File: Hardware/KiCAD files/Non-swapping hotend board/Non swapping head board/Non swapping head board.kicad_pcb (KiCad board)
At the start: 2 copper layers, 21.6 x 31.7 mm, 4 parts, among them J1 JST_06, J18 JST_1mm_3_Vertical, J20 PINHD_1x10_Female, J22 Conn_01x02

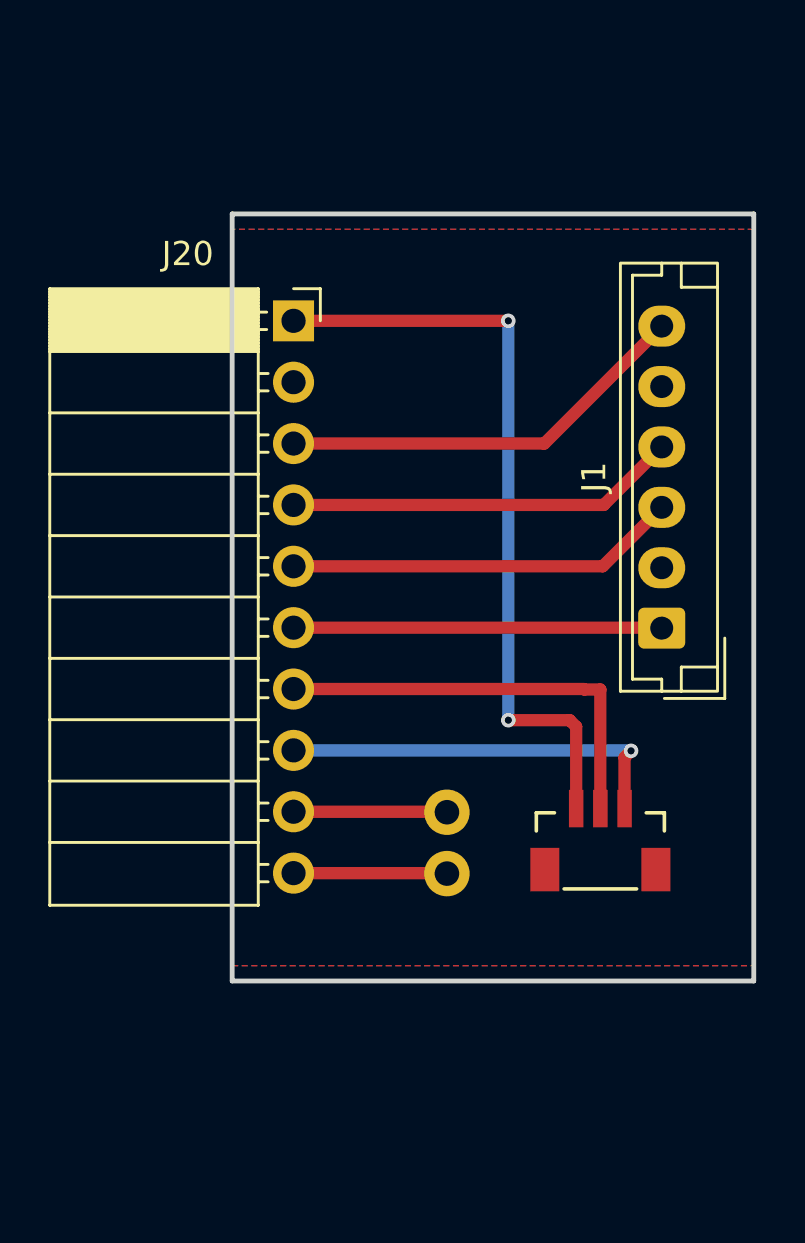
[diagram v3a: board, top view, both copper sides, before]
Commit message: Compatability mods
basic modifications to work toward compatability between boards physically on the hotend
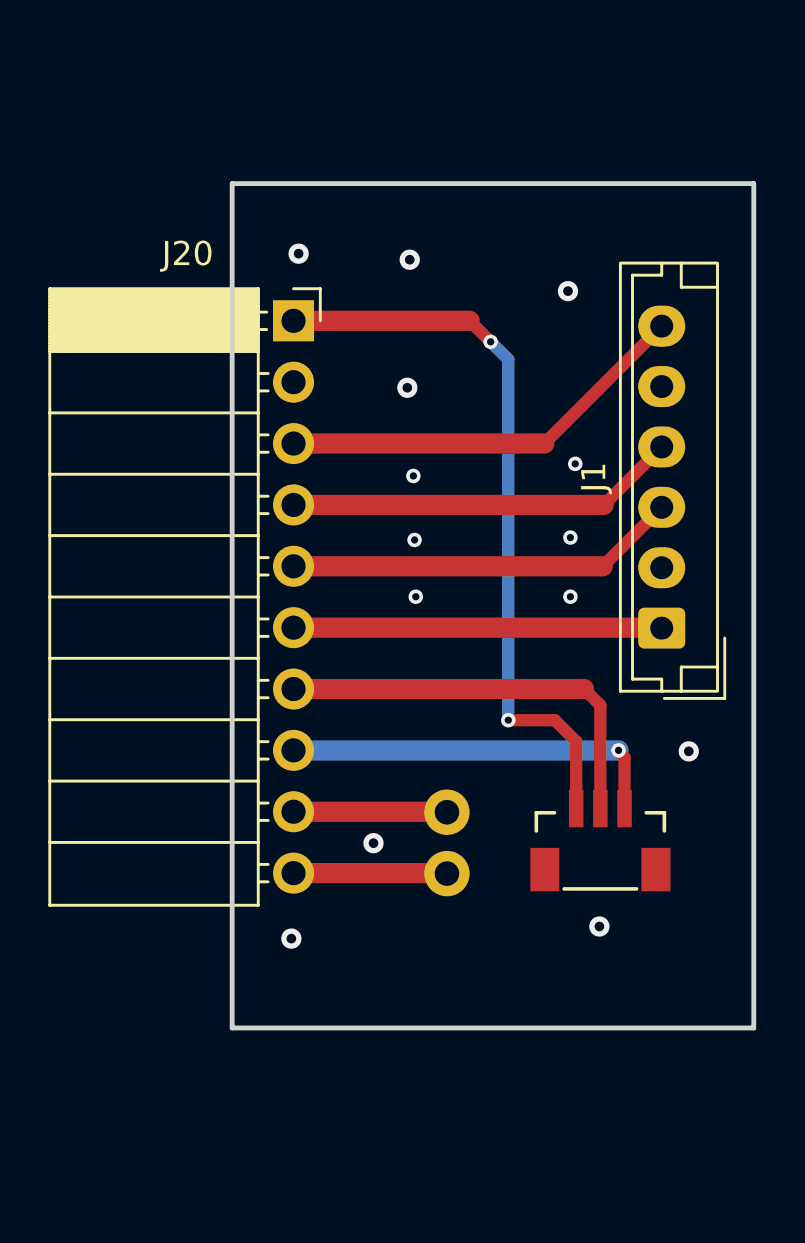
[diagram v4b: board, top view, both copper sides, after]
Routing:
- net Net-(J18-Pad3): track 31.7 -> 30.4 mm
- net Net-(J18-Pad1): track 16.5 -> 16.0 mm
- net GND: vias 0 -> 14
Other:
- board size 21.6 x 31.7 mm -> 21.6 x 35 mm
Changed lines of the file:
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@@
 	)
 	(gr_rect
-		(start 95.25 40.005)
-		(end 116.84 71.755)
+		(start 95.25 38.75)
+		(end 116.84 73.7)
 		(stroke
 			(width 0.2)
@@
 	)
 	(segment
-		(start 109.49 61.23)
-		(end 109.22 60.96)
-		(width 0.508)
-		(layer "F.Cu")
-		(net "Net-(J18-Pad3)")
-	)
-	(segment
-		(start 109.22 60.96)
+		(start 105.95 45.3)
+		(end 105.08 44.43)
+		(width 0.508)
+		(layer "F.Cu")
+		(net "Net-(J18-Pad3)")
+	)
+	(segment
+		(start 105.08 44.43)
+		(end 97.79 44.43)
+		(width 0.8382)
+		(layer "F.Cu")
+		(net "Net-(J18-Pad3)")
+	)
+	(segment
+		(start 109.49 64.6185)
+		(end 109.49 61.84)
+		(width 0.508)
+		(layer "F.Cu")
+		(net "Net-(J18-Pad3)")
+	)
+	(segment
+		(start 109.49 61.84)
+		(end 108.61 60.96)
+		(width 0.508)
+		(layer "F.Cu")
+		(net "Net-(J18-Pad3)")
+	)
+	(segment
+		(start 108.61 60.96)
 		(end 106.68 60.96)
 		(width 0.508)
@@
 		(net "Net-(J18-Pad3)")
 	)
-	(segment
-		(start 106.68 44.43)
-		(end 97.79 44.43)
-		(width 0.508)
-		(layer "F.Cu")
-		(net "Net-(J18-Pad3)")
-	)
-	(segment
-		(start 109.49 64.6185)
-		(end 109.49 61.23)
-		(width 0.508)
-		(layer "F.Cu")
-		(net "Net-(J18-Pad3)")
-	)
 	(via
 		(at 106.68 60.96)
@@
 	)
 	(via
-		(at 106.68 44.43)
-		(size 0.6)
-		(drill 0.3)
-		(layers "F.Cu" "B.Cu")
-		(net "Net-(J18-Pad3)")
-	)
-	(segment
-		(start 106.68 44.43)
+		(at 105.95 45.3)
+		(size 0.6)
+		(drill 0.3)
+		(layers "F.Cu" "B.Cu")
+		(net "Net-(J18-Pad3)")
+	)
+	(segment
+		(start 106.68 46.03)
 		(end 106.68 60.96)
 		(width 0.508)
 		(layer "B.Cu")
 		(net "Net-(J18-Pad3)")
+	)
+	(segment
+		(start 105.95 45.3)
+		(end 106.68 46.03)
+		(width 0.508)
+		(layer "B.Cu")
+		(net "Net-(J18-Pad3)")
+	)
+	(via
+		(at 110.45 69.5)
+		(size 0.8382)
+		(drill 0.4)
+		(layers "F.Cu" "B.Cu")
+		(free yes)
+		(net "GND")
+	)
+	(via
+		(at 97.7 70)
+		(size 0.8382)
+		(drill 0.4)
+		(layers "F.Cu" "B.Cu")
+		(free yes)
+		(net "GND")
+	)
+	(via
+		(at 109.25 55.85)
+		(size 0.6)
+		(drill 0.3)
+		(layers "F.Cu" "B.Cu")
+		(free yes)
+		(net "GND")
+	)
+	(via
+		(at 102.85 55.85)
+		(size 0.6)
+		(drill 0.3)
+		(layers "F.Cu" "B.Cu")
+		(free yes)
+		(net "GND")
+	)
+	(via
+		(at 102.6 41.9)
+		(size 0.8382)
+		(drill 0.4)
+		(layers "F.Cu" "B.Cu")
+		(free yes)
+		(net "GND")
+	)
+	(via
+		(at 98 41.65)
+		(size 0.8382)
+		(drill 0.4)
+		(layers "F.Cu" "B.Cu")
+		(free yes)
+		(net "GND")
+	)
+	(via
+		(at 114.15 62.25)
+		(size 0.8382)
+		(drill 0.4)
+		(layers "F.Cu" "B.Cu")
+		(free yes)
+		(net "GND")
+	)
+	(via
+		(at 102.8 53.5)
+		(size 0.6)
+		(drill 0.3)
+		(layers "F.Cu" "B.Cu")
+		(free yes)
+		(net "GND")
+	)
+	(via
+		(at 109.45 50.35)
+		(size 0.6)
+		(drill 0.3)
+		(layers "F.Cu" "B.Cu")
+		(free yes)
+		(net "GND")
+	)
+	(via
+		(at 109.25 53.4)
+		(size 0.6)
+		(drill 0.3)
+		(layers "F.Cu" "B.Cu")
+		(free yes)
+		(net "GND")
+	)
+	(via
+		(at 101.1 66.05)
+		(size 0.8382)
+		(drill 0.4)
+		(layers "F.Cu" "B.Cu")
+		(free yes)
+		(net "GND")
+	)
+	(via
+		(at 109.15 43.2)
+		(size 0.8382)
+		(drill 0.4)
+		(layers "F.Cu" "B.Cu")
+		(free yes)
+		(net "GND")
+	)
+	(via
+		(at 102.75 50.85)
+		(size 0.6)
+		(drill 0.3)
+		(layers "F.Cu" "B.Cu")
+		(free yes)
+		(net "GND")
+	)
+	(via
+		(at 102.5 47.2)
+		(size 0.8382)
+		(drill 0.4)
+		(layers "F.Cu" "B.Cu")
+		(free yes)
+		(net "GND")
 	)
 	(segment
 		(start 108.17 49.51)
 		(end 97.79 49.51)
-		(width 0.508)
+		(width 0.8382)
 		(layer "F.Cu")
 		(net "/A1")
@@
 		(start 110.63 52.05)
 		(end 97.79 52.05)
-		(width 0.508)
+		(width 0.8382)
 		(layer "F.Cu")
 		(net "/B1")
@@
 		(start 110.59 54.59)
 		(end 97.79 54.59)
-		(width 0.508)
+		(width 0.8382)
 		(layer "F.Cu")
 		(net "/A2")
@@
 		(start 113.01 57.13)
 		(end 97.79 57.13)
-		(width 0.508)
+		(width 0.8382)
 		(layer "F.Cu")
 		(net "/B2")
@@
 	)
 	(segment
-		(start 110.49 59.69)
+		(start 109.84 59.69)
 		(end 109.83 59.69)
+		(width 0.508)
+		(layer "F.Cu")
+		(net "Net-(J18-Pad2)")
+	)
+	(segment
+		(start 110.49 60.34)
+		(end 109.84 59.69)
+		(width 0.508)
+		(layer "F.Cu")
+		(net "Net-(J18-Pad2)")
+	)
+	(segment
+		(start 109.81 59.67)
+		(end 97.79 59.67)
+		(width 0.8382)
+		(layer "F.Cu")
+		(net "Net-(J18-Pad2)")
+	)
+	(segment
+		(start 110.49 64.6185)
+		(end 110.49 60.34)
 		(width 0.508)
 		(layer "F.Cu")
@@
 	)
 	(segment
-		(start 109.81 59.67)
-		(end 97.79 59.67)
-		(width 0.508)
-		(layer "F.Cu")
-		(net "Net-(J18-Pad2)")
-	)
-	(segment
-		(start 110.49 64.6185)
-		(end 110.49 59.69)
-		(width 0.508)
-		(layer "F.Cu")
-		(net "Net-(J18-Pad2)")
-	)
-	(segment
-		(start 111.49 64.6185)
+		(start 111.244 62.21)
+		(end 111.244 62.254)
+		(width 0.508)
+		(layer "F.Cu")
+		(net "Net-(J18-Pad1)")
+	)
+	(segment
+		(start 111.49 62.5)
+		(end 111.49 64.6185)
+		(width 0.508)
+		(layer "F.Cu")
+		(net "Net-(J18-Pad1)")
+	)
+	(segment
+		(start 111.244 62.254)
 		(end 111.49 62.5)
 		(width 0.508)
@@
 		(net "Net-(J18-Pad1)")
 	)
-	(segment
-		(start 111.49 62.5)
-		(end 111.76 62.23)
-		(width 0.508)
-		(layer "F.Cu")
-		(net "Net-(J18-Pad1)")
-	)
-	(via
-		(at 111.76 62.23)
-		(size 0.6)
-		(drill 0.3)
-		(layers "F.Cu" "B.Cu")
-		(net "Net-(J18-Pad1)")
-	)
-	(segment
-		(start 111.74 62.21)
+	(via
+		(at 111.244 62.21)
+		(size 0.6)
+		(drill 0.3)
+		(layers "F.Cu" "B.Cu")
+		(net "Net-(J18-Pad1)")
+	)
+	(segment
+		(start 111.244 62.21)
 		(end 97.79 62.21)
-		(width 0.508)
-		(layer "B.Cu")
-		(net "Net-(J18-Pad1)")
-	)
-	(segment
-		(start 111.76 62.23)
-		(end 111.74 62.21)
-		(width 0.508)
+		(width 0.8382)
 		(layer "B.Cu")
 		(net "Net-(J18-Pad1)")
@@
 		(start 104.12 64.75)
 		(end 97.79 64.75)
-		(width 0.508)
+		(width 0.8382)
 		(layer "F.Cu")
 		(net "Net-(J22-Pin_2)")
@@
 		(start 104.12 67.29)
 		(end 97.79 67.29)
-		(width 0.508)
+		(width 0.8382)
 		(layer "F.Cu")
 		(net "Net-(J22-Pin_1)")
@@
 		(polygon
 			(pts
-				(xy 116.84 40.64) (xy 95.25 40.64) (xy 95.25 71.12) (xy 116.84 71.12)
+				(xy 116.84 38.75) (xy 95.25 38.75) (xy 95.25 73.7) (xy 116.84 73.7)
 			)
 		)

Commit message: V1 boards after final board invoice
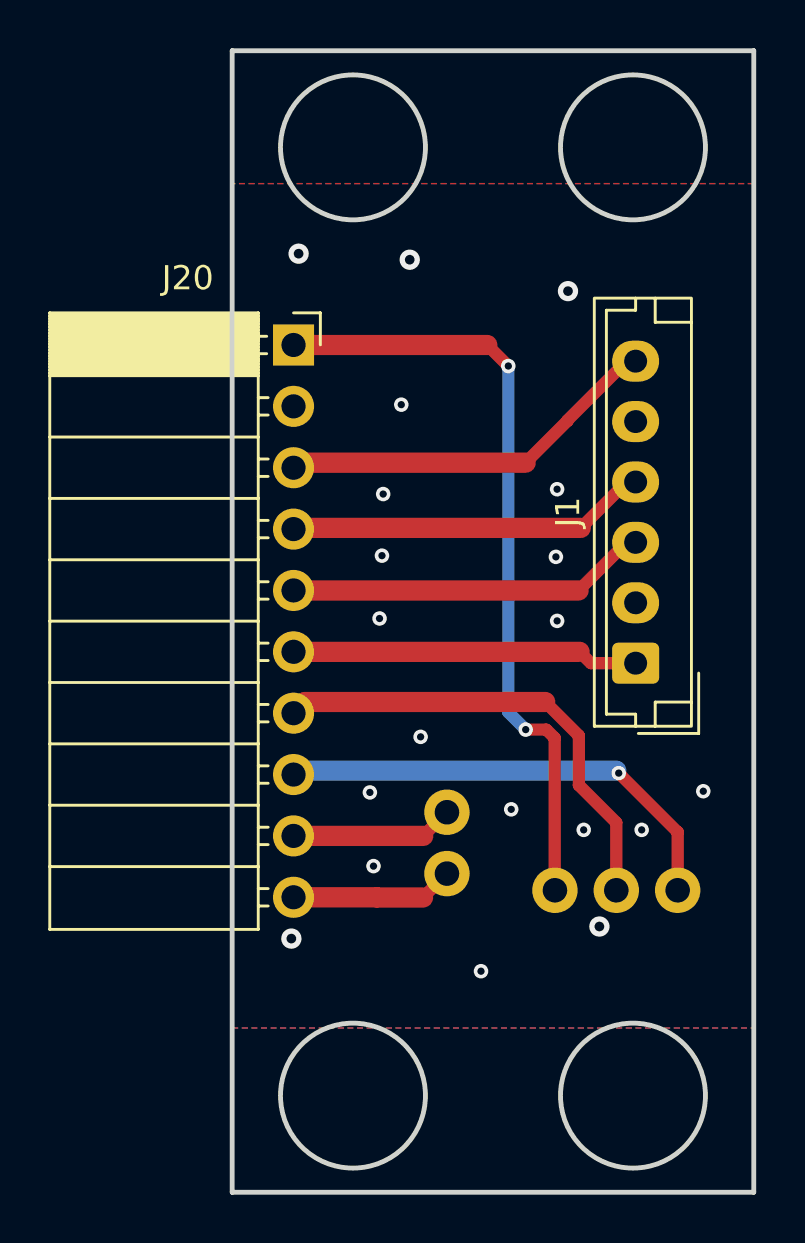
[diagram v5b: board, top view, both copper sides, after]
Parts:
- J18: footprint PCM_SparkFun-Connector:JST_1x03_P1.0mm_Vertical_SMD -> PCM_SparkFun-Connector:1x03_P2.54mm
- moved J18 3.20 mm to (113.7, 68.0)
- moved J1 1.81 mm to (112.0, 58.6)
- moved J20 1.00 mm to (97.8, 45.4)
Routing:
- net Net-(J18-Pad1): track 16.0 -> 19.4 mm
- net Net-(J18-Pad2): track 17.3 -> 19.6 mm
- net Net-(J18-Pad3): track 30.4 -> 31.8 mm
- net /A1: track 17.3 -> 16.0 mm
- net /B1: track 16.2 -> 15.0 mm
- net /A2: track 16.3 -> 15.0 mm
- net /B2: track 15.2 -> 14.4 mm
- net GND: track 0.00 -> 0.06 mm, vias 14 -> 20
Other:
- board size 21.6 x 35 mm -> 21.6 x 47.2 mm
